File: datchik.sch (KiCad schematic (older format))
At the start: 0 parts

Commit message: добавлен разьем програмирования
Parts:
- added P?: CONN_5, symbol CONN_5
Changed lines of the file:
@@
 LIBS:contrib
 LIBS:valves
+LIBS:datchik-cache
 EELAYER 27 0
 EELAYER END
@@
 Comment4 ""
 $EndDescr
+$Comp
+L CONN_5 P?
+U 1 1 545221CE
+P 900 1100
+F 0 "P?" V 850 1100 50  0000 C CNN
+F 1 "CONN_5" V 950 1100 50  0000 C CNN
+F 2 "" H 900 1100 60  0000 C CNN
+F 3 "" H 900 1100 60  0000 C CNN
+	1    900  1100
+	-1   0    0    1
+$EndComp
+Wire Bus Line
+	1500 750  1500 1600
+Entry Wire Line
+	1400 1300 1500 1400
+Entry Wire Line
+	1400 1200 1500 1300
+Entry Wire Line
+	1400 1100 1500 1200
+Entry Wire Line
+	1400 900  1500 1000
+Entry Wire Line
+	1400 1000 1500 1100
+Wire Wire Line
+	1300 900  1400 900
+Wire Wire Line
+	1300 1000 1400 1000
+Wire Wire Line
+	1300 1100 1400 1100
+Wire Wire Line
+	1300 1200 1400 1200
+Wire Wire Line
+	1300 1300 1400 1300
+Text Label 1200 1300 0    60   ~ 0
+VCC
+Text Label 1200 1200 0    60   ~ 0
+swclk
+Text Label 1200 1100 0    60   ~ 0
+swdat
+Text Label 1200 1000 0    60   ~ 0
+reset
+Text Label 1200 900  0    60   ~ 0
+GND
 $EndSCHEMATC

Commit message: добавлена печатная плата
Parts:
- added C1: CAPAPOL, ~, symbol CAPAPOL
- gave numbers to parts that had none: 1
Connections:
- net GND: now also P1.5, C1.2
- net VCC: now also P1.1, C1.1
- net reset: now also P1.4
- net swclk: now also P1.2
- net swdat: now also P1.3
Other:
- moved on the sheet: P1
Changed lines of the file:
@@
 $EndDescr
 $Comp
-L CONN_5 P?
+L CONN_5 P1
 U 1 1 545221CE
-P 900 1100
-F 0 "P?" V 850 1100 50  0000 C CNN
-F 1 "CONN_5" V 950 1100 50  0000 C CNN
-F 2 "" H 900 1100 60  0000 C CNN
-F 3 "" H 900 1100 60  0000 C CNN
-	1    900  1100
+P 650 1100
+F 0 "P1" V 600 1100 50  0000 C CNN
+F 1 "CONN_5" V 700 1100 50  0000 C CNN
+F 2 "" H 650 1100 60  0000 C CNN
+F 3 "" H 650 1100 60  0000 C CNN
+	1    650  1100
 	-1   0    0    1
 $EndComp
@@
 	1400 1000 1500 1100
 Wire Wire Line
-	1300 900  1400 900
+	1050 900  1400 900
 Wire Wire Line
-	1300 1000 1400 1000
+	1050 1000 1400 1000
 Wire Wire Line
-	1300 1100 1400 1100
+	1050 1100 1400 1100
 Wire Wire Line
-	1300 1200 1400 1200
+	1050 1200 1400 1200
 Wire Wire Line
-	1300 1300 1400 1300
-Text Label 1200 1300 0    60   ~ 0
+	1050 1300 1400 1300
+Text Label 1150 1300 0    60   ~ 0
 VCC
-Text Label 1200 1200 0    60   ~ 0
+Text Label 1150 1200 0    60   ~ 0
 swclk
-Text Label 1200 1100 0    60   ~ 0
+Text Label 1150 1100 0    60   ~ 0
 swdat
-Text Label 1200 1000 0    60   ~ 0
+Text Label 1150 1000 0    60   ~ 0
 reset
-Text Label 1200 900  0    60   ~ 0
+Text Label 1150 900  0    60   ~ 0
+GND
+$Comp
+L CAPAPOL C1
+U 1 1 54522450
+P 1750 1150
+F 0 "C1" H 1800 1250 40  0000 L CNN
+F 1 "CAPAPOL" H 1800 1050 40  0000 L CNN
+F 2 "~" H 1850 1000 30  0000 C CNN
+F 3 "~" H 1750 1150 300 0000 C CNN
+	1    1750 1150
+	1    0    0    -1
+$EndComp
+Entry Wire Line
+	1500 1250 1600 1350
+Entry Wire Line
+	1500 850  1600 950
+Wire Wire Line
+	1600 950  1750 950
+Wire Wire Line
+	1600 1350 1750 1350
+Text Label 1650 950  0    60   ~ 0
+VCC
+Text Label 1650 1350 3    60   ~ 0
 GND
 $EndSCHEMATC

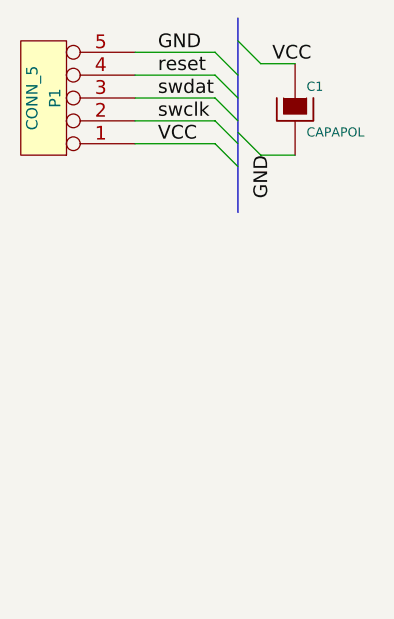
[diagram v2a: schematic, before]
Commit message: добавлен кварц и кондеры
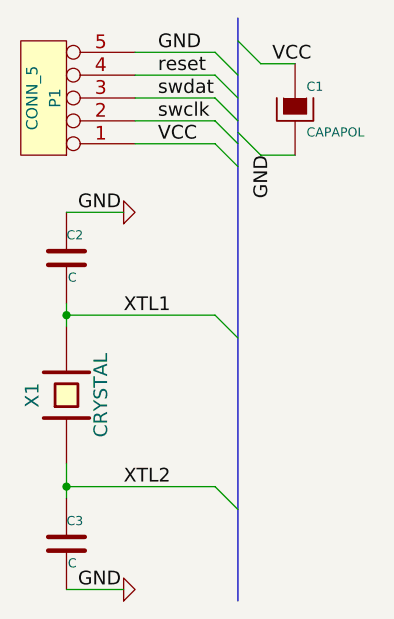
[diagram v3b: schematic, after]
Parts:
- added C2, C3: C, ~, symbol C
- added X1: CRYSTAL, ~, symbol CRYSTAL
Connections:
- net GND: now also C2.1, C3.2
- new net XTL1: C2.2, X1.2
- new net XTL2: C3.1, X1.1
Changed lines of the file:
@@
 $EndComp
 Wire Bus Line
-	1500 750  1500 1600
+	1500 750  1500 3300
 Entry Wire Line
 	1400 1300 1500 1400
@@
 Text Label 1650 1350 3    60   ~ 0
 GND
+$Comp
+L CRYSTAL X1
+U 1 1 5452290C
+P 750 2400
+F 0 "X1" H 750 2550 60  0000 C CNN
+F 1 "CRYSTAL" H 750 2250 60  0000 C CNN
+F 2 "~" H 750 2400 60  0000 C CNN
+F 3 "~" H 750 2400 60  0000 C CNN
+	1    750  2400
+	0    -1   -1   0
+$EndComp
+$Comp
+L C C2
+U 1 1 54522929
+P 750 1800
+F 0 "C2" H 750 1900 40  0000 L CNN
+F 1 "C" H 756 1715 40  0000 L CNN
+F 2 "~" H 788 1650 30  0000 C CNN
+F 3 "~" H 750 1800 60  0000 C CNN
+	1    750  1800
+	1    0    0    -1
+$EndComp
+$Comp
+L C C3
+U 1 1 54522938
+P 750 3050
+F 0 "C3" H 750 3150 40  0000 L CNN
+F 1 "C" H 756 2965 40  0000 L CNN
+F 2 "~" H 788 2900 30  0000 C CNN
+F 3 "~" H 750 3050 60  0000 C CNN
+	1    750  3050
+	1    0    0    -1
+$EndComp
+Wire Wire Line
+	750  2000 750  2100
+Wire Wire Line
+	750  2700 750  2850
+Entry Wire Line
+	1400 2050 1500 2150
+Entry Wire Line
+	1400 2800 1500 2900
+Wire Wire Line
+	1400 2050 750  2050
+Connection ~ 750  2050
+Wire Wire Line
+	750  2800 1400 2800
+Connection ~ 750  2800
+$Comp
+L GND #PWR1
+U 1 1 54522992
+P 1000 1600
+F 0 "#PWR1" H 1000 1600 30  0001 C CNN
+F 1 "GND" H 1000 1530 30  0001 C CNN
+F 2 "" H 1000 1600 60  0000 C CNN
+F 3 "" H 1000 1600 60  0000 C CNN
+	1    1000 1600
+	0    -1   -1   0
+$EndComp
+$Comp
+L GND #PWR2
+U 1 1 545229A1
+P 1000 3250
+F 0 "#PWR2" H 1000 3250 30  0001 C CNN
+F 1 "GND" H 1000 3180 30  0001 C CNN
+F 2 "" H 1000 3250 60  0000 C CNN
+F 3 "" H 1000 3250 60  0000 C CNN
+	1    1000 3250
+	0    -1   -1   0
+$EndComp
+Wire Wire Line
+	1000 1600 750  1600
+Wire Wire Line
+	1000 3250 750  3250
+Text Label 800  1600 0    60   ~ 0
+GND
+Text Label 800  3250 0    60   ~ 0
+GND
+Text Label 1000 2050 0    60   ~ 0
+XTL1
+Text Label 1000 2800 0    60   ~ 0
+XTL2
 $EndSCHEMATC

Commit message: добавлены кондесаторы фильтра
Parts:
- added C4, C5: C, ~, symbol C
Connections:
- net GND: now also C4.2, C5.2
- net VCC: now also C4.1, C5.1
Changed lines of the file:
@@
 Text Label 1000 2800 0    60   ~ 0
 XTL2
+$Comp
+L C C4
+U 1 1 54522B0A
+P 1700 1850
+F 0 "C4" H 1700 1950 40  0000 L CNN
+F 1 "C" H 1706 1765 40  0000 L CNN
+F 2 "~" H 1738 1700 30  0000 C CNN
+F 3 "~" H 1700 1850 60  0000 C CNN
+	1    1700 1850
+	1    0    0    -1
+$EndComp
+$Comp
+L C C5
+U 1 1 54522B19
+P 1700 2550
+F 0 "C5" H 1700 2650 40  0000 L CNN
+F 1 "C" H 1706 2465 40  0000 L CNN
+F 2 "~" H 1738 2400 30  0000 C CNN
+F 3 "~" H 1700 2550 60  0000 C CNN
+	1    1700 2550
+	1    0    0    -1
+$EndComp
+Entry Wire Line
+	1500 1550 1600 1650
+Entry Wire Line
+	1500 1950 1600 2050
+Entry Wire Line
+	1500 2250 1600 2350
+Entry Wire Line
+	1500 2650 1600 2750
+Wire Wire Line
+	1600 1650 1700 1650
+Wire Wire Line
+	1600 2050 1700 2050
+Wire Wire Line
+	1600 2350 1700 2350
+Wire Wire Line
+	1600 2750 1700 2750
+Text Label 1600 1650 0    60   ~ 0
+VCC
+Text Label 1650 2050 0    60   ~ 0
+GND
+Text Label 1650 2350 0    60   ~ 0
+VCC
+Text Label 1650 2750 0    60   ~ 0
+GND
 $EndSCHEMATC

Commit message: датчик пыли
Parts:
- added D1: LED, ~, symbol LED
- added P2: CONN_5X2, symbol CONN_5X2
- added Q1: OPTO_NPN, ~, symbol OPTO_NPN
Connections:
- net labels added: USB_DM, USB_DP, VCC_USB
- wire segments 17 -> 33
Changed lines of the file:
@@
 $EndComp
 Wire Bus Line
-	1500 750  1500 3300
+	1500 750  1500 3600
 Entry Wire Line
 	1400 1300 1500 1400
@@
 Text Label 1650 2750 0    60   ~ 0
 GND
+$Comp
+L CONN_5X2 P2
+U 1 1 54522D68
+P 1550 4100
+F 0 "P2" H 1550 4400 60  0000 C CNN
+F 1 "CONN_5X2" V 1550 4100 50  0000 C CNN
+F 2 "" H 1550 4100 60  0000 C CNN
+F 3 "" H 1550 4100 60  0000 C CNN
+	1    1550 4100
+	1    0    0    -1
+$EndComp
+Wire Bus Line
+	1500 3600 2500 3600
+Wire Bus Line
+	2500 3600 2500 4650
+Wire Bus Line
+	2500 4650 650  4650
+Wire Bus Line
+	650  3650 650  5850
+Entry Wire Line
+	650  3800 750  3900
+Entry Wire Line
+	650  3900 750  4000
+Entry Wire Line
+	650  4000 750  4100
+Entry Wire Line
+	650  4200 750  4300
+Entry Wire Line
+	650  4100 750  4200
+Wire Wire Line
+	750  3900 1150 3900
+Wire Wire Line
+	750  4000 1150 4000
+Wire Wire Line
+	750  4100 1150 4100
+Wire Wire Line
+	750  4200 1150 4200
+Wire Wire Line
+	750  4300 1150 4300
+Entry Wire Line
+	2400 3900 2500 4000
+Entry Wire Line
+	2400 4000 2500 4100
+Entry Wire Line
+	2400 4100 2500 4200
+Entry Wire Line
+	2400 4200 2500 4300
+Entry Wire Line
+	2400 4300 2500 4400
+Wire Wire Line
+	2400 3900 1950 3900
+Wire Wire Line
+	2400 4000 1950 4000
+Wire Wire Line
+	2400 4100 1950 4100
+Wire Wire Line
+	2400 4200 1950 4200
+Wire Wire Line
+	2400 4300 1950 4300
+Text Label 800  3900 0    60   ~ 0
+USB_DP
+Text Label 800  4000 0    60   ~ 0
+USB_DM
+Text Label 800  4100 0    60   ~ 0
+GND
+Text Label 800  4200 0    60   ~ 0
+VCC_USB
+$Comp
+L LED D1
+U 1 1 54522FA6
+P 900 5000
+F 0 "D1" H 900 5100 50  0000 C CNN
+F 1 "LED" H 900 4900 50  0000 C CNN
+F 2 "~" H 900 5000 60  0000 C CNN
+F 3 "~" H 900 5000 60  0000 C CNN
+	1    900  5000
+	0    -1   -1   0
+$EndComp
+$Comp
+L OPTO_NPN Q1
+U 1 1 54522FB5
+P 1300 5000
+F 0 "Q1" H 1450 5050 50  0000 L CNN
+F 1 "OPTO_NPN" H 1450 4900 50  0000 L CNN
+F 2 "~" H 1300 5000 60  0000 C CNN
+F 3 "~" H 1300 5000 60  0000 C CNN
+	1    1300 5000
+	1    0    0    -1
+$EndComp
+Entry Wire Line
+	650  5100 750  5200
+Entry Wire Line
+	650  4700 750  4800
+Wire Wire Line
+	900  5200 750  5200
+Wire Wire Line
+	900  4800 750  4800
+Entry Wire Line
+	650  5200 750  5300
+Entry Wire Line
+	1000 4650 1100 4750
+Wire Wire Line
+	750  5300 1400 5300
+Wire Wire Line
+	1400 5300 1400 5200
+Wire Wire Line
+	1100 4750 1400 4750
+Wire Wire Line
+	1400 4750 1400 4800
+Wire Notes Line
+	1500 4750 750  4750
+Wire Notes Line
+	750  4750 750  5350
+Wire Notes Line
+	750  5350 1500 5350
+Wire Notes Line
+	1500 5350 1500 4750
 $EndSCHEMATC
